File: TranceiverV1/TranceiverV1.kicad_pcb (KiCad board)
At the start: 2 copper layers, 94.6 x 45.6 mm, 19 parts, among them J1 Conn_01x03_Socket, J3 Battery, U1 NRF24L01_, U3 102010388, U4 LD1086DTTR

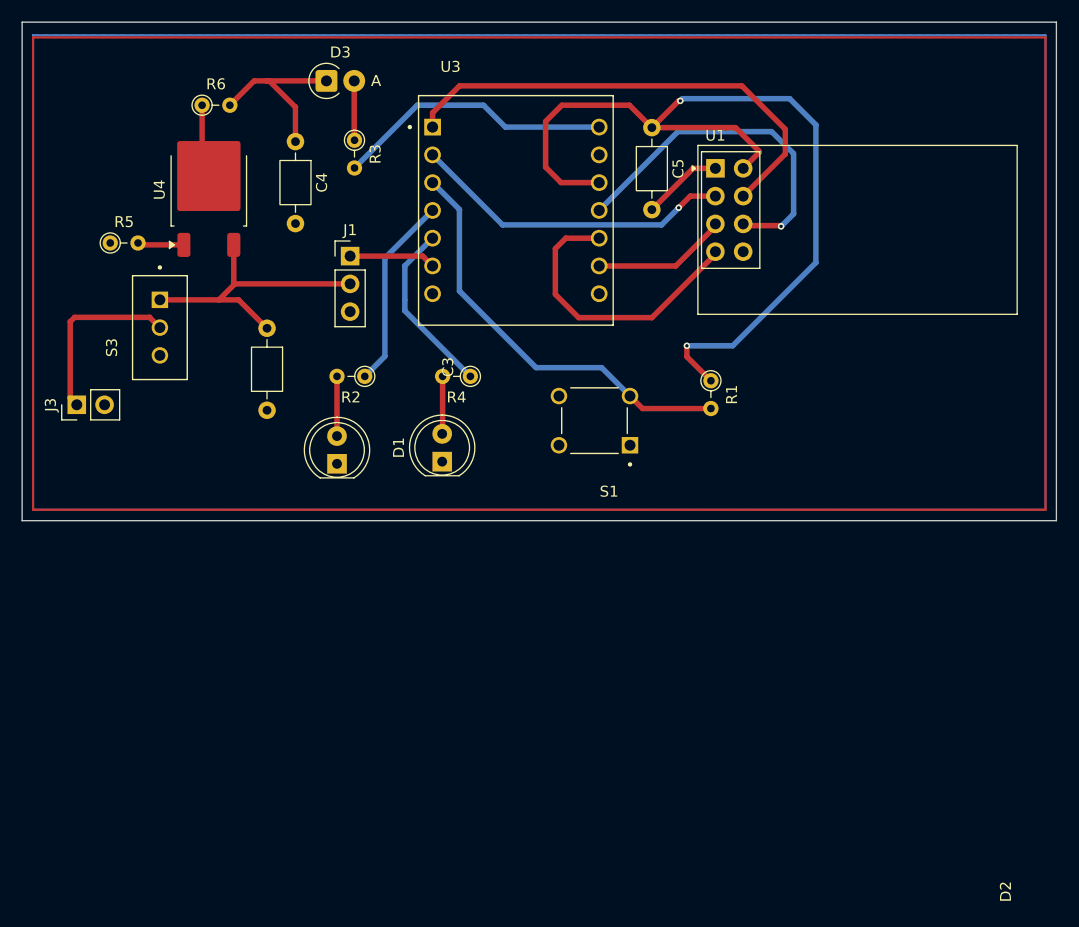
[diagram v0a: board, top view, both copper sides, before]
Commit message: rewired traces and changed diode position added mounting holes
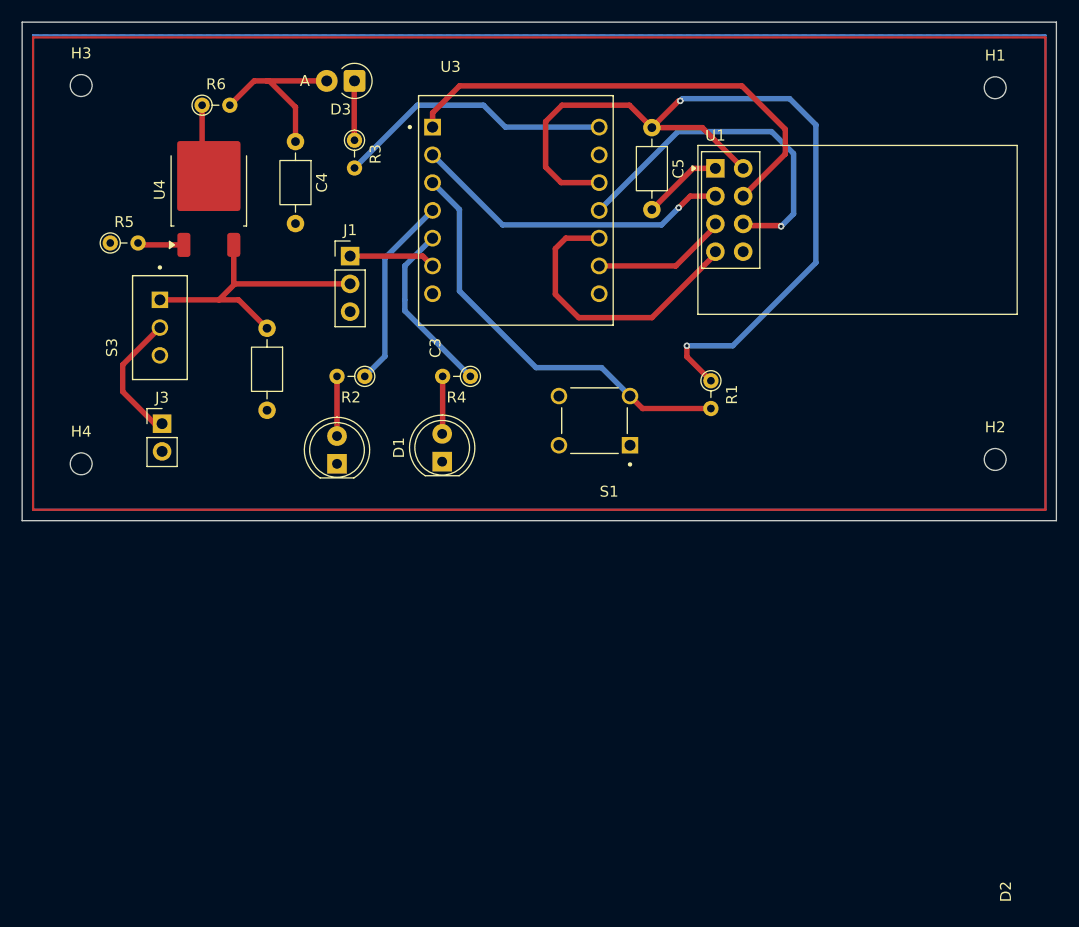
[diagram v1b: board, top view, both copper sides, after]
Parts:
- added H1: MountingHole, MountingHole:MountingHole_2mm, F.Cu at (202.6, 107.6)
- added H2: MountingHole, MountingHole:MountingHole_2mm, F.Cu at (202.6, 141.6)
- added H3: MountingHole, MountingHole:MountingHole_2mm, F.Cu at (119.0, 107.4)
- added H4: MountingHole, MountingHole:MountingHole_2mm, F.Cu at (119.0, 142.0)
- moved J3 7.99 mm to (126.4, 138.3), turned to 0 degrees
- moved D3 2.56 mm to (144.0, 107.0), turned to 180 degrees
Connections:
- C4 pad 1: Net-(D3-K) -> Net-(D3-A)
- R3 pad 1: Net-(D3-A) -> Net-(D3-K)
- R6 pad 2: Net-(D3-K) -> Net-(D3-A)
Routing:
- net Net-(D3-K): track 16.5 -> 5.44 mm
- net Net-(D3-A): track 5.44 -> 16.5 mm
- net Net-(J3-Pin_1): track 16.6 -> 12.1 mm
- net /VCC: track 82.5 -> 79.5 mm
